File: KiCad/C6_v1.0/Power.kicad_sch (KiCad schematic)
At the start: 35 parts, among them J6 6130XX11121_61300511121, J7 Conn_01x05_Pin

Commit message: pingus
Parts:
- removed C20: WCAP-ASLL_4X5.5/865060640001 1uf smd electrolytic, 865060640001 1uf electrolytic:WCAP-ASLL_4X5.5_DXL_, symbol WCAP-ASLL_4X5.5:WCAP-ASLL_4X5.5
- removed C?: WCAP-ASLI_5X5.5/ 47uf electro, 865080342006 47uf electrolytic:WCAP-ASLI_5X5.5_DXL_, symbol WCAP-ASLI_5X5.5:WCAP-ASLI_5X5.5
- removed J7: Conn_01x05_Pin, Connector_PinHeader_2.00mm:PinHeader_1x05_P2.00mm_Vertical, symbol Connector:Conn_01x05_Pin
- removed Payload_Header?: B02B-XASK-1LFSN, footprints:CONN_B02B-XASK-1LFSN_JST, symbol 2025-10-14_01-11-02:B02B-XASK-1LFSN
- removed Payload_LoadSwitch?: TPS22919DCKR, TPS22919DCKR:SOT65P210X110-6N, symbol TPS22919DCKR:TPS22919DCKR
- removed R33: RC0201FR-0710KL/ 10k, Resistor_SMD:R_0201_0603Metric_Pad0.64x0.40mm_HandSolder, symbol 2025-10-26_02-06-39:RC0201FR-0710KL
- removed R38: RC0402JR-071KL 1k, Resistor_SMD:R_0402_1005Metric_Pad0.72x0.64mm_HandSolder, symbol 2025-10-26_18-21-17:RC0402JR-071KL
- R33: renamed from R?; value 10000 -> 51k
- gave numbers to parts that had none: 17
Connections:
- no-connect marks 3 -> 1
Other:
- moved on the sheet: J6, R33, TP1

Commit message: yay
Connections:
- net +2.8V is gone; now on net 2V8: J6.2
- net +3.3V is gone; now on net 3V3: J6.3
- net +5V is gone; now on net 5V: C35.1, C37.1, Current_Monitor1.1 (A1), Current_Monitor1.2 (A0), Current_Monitor1.5 (VS), J6.4
- net +8.4V is gone; now on net 8V4: J6.5
- net 1.8V is gone; now on net 1V8: J6.1
- net ADC_IN renamed ADC
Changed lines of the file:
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@@
+	(wire
+		(pts
+			(xy 222.25 78.74) (xy 233.68 78.74)
+		)
+		(stroke
+			(width 0)
+			(type default)
+		)
+	)
 	(wire
 		(pts
@@
 	(wire
 		(pts
-			(xy 224.79 81.28) (xy 233.68 81.28)
-		)
-		(stroke
-			(width 0)
-			(type default)
-		)
-	)
-	(wire
-		(pts
 			(xy 185.42 137.16) (xy 201.93 137.16)
 		)
@@
 	(wire
 		(pts
-			(xy 224.79 78.74) (xy 233.68 78.74)
-		)
-		(stroke
-			(width 0)
-			(type default)
-		)
-	)
-	(wire
-		(pts
 			(xy 59.69 146.05) (xy 67.31 146.05)
 		)
@@
 		(pts
 			(xy 49.53 153.67) (xy 49.53 157.48)
+		)
+		(stroke
+			(width 0)
+			(type default)
+		)
+	)
+	(wire
+		(pts
+			(xy 222.25 81.28) (xy 233.68 81.28)
 		)
 		(stroke
@@
 		)
 	)
+	(label "8V4"
+		(at 123.19 30.48 270)
+		(effects
+			(font
+				(size 1.27 1.27)
+			)
+			(justify right bottom)
+		)
+	)
+	(label "2V8"
+		(at 115.57 30.48 270)
+		(effects
+			(font
+				(size 1.27 1.27)
+			)
+			(justify right bottom)
+		)
+	)
+	(label "3V3"
+		(at 118.11 30.48 270)
+		(effects
+			(font
+				(size 1.27 1.27)
+			)
+			(justify right bottom)
+		)
+	)
 	(label "VOUT"
 		(at 231.14 88.9 180)
@@
 		)
 	)
+	(label "1V8"
+		(at 113.03 30.48 270)
+		(effects
+			(font
+				(size 1.27 1.27)
+			)
+			(justify right bottom)
+		)
+	)
+	(label "5V"
+		(at 93.98 73.66 0)
+		(effects
+			(font
+				(size 1.27 1.27)
+			)
+			(justify left bottom)
+		)
+	)
 	(label "bruh"
 		(at 195.58 137.16 0)
@@
 		)
 	)
-	(global_label "EGSE_TX"
-		(shape input)
-		(at 224.79 81.28 180)
-		(fields_autoplaced yes)
-		(effects
-			(font
-				(size 1.27 1.27)
-			)
-			(justify right)
-		)
-		(property "Intersheetrefs" "${INTERSHEET_REFS}"
-			(at 213.8826 81.28 0)
-			(effects
-				(font
-					(size 1.27 1.27)
-				)
-				(justify right)
-				(hide yes)
-			)
-		)
-	)
-	(global_label "+8.4V"
-		(shape input)
-		(at 123.19 30.48 270)
-		(fields_autoplaced yes)
-		(effects
-			(font
-				(size 1.27 1.27)
-			)
-			(justify right)
-		)
-		(property "Intersheetrefs" "${INTERSHEET_REFS}"
-			(at 123.19 39.15 90)
-			(effects
-				(font
-					(size 1.27 1.27)
-				)
-				(justify right)
-				(hide yes)
-			)
-		)
-	)
-	(global_label "I2C_SCL"
-		(shape input)
-		(at 104.14 99.06 0)
-		(fields_autoplaced yes)
-		(effects
-			(font
-				(size 1.27 1.27)
-			)
-			(justify left)
-		)
-		(property "Intersheetrefs" "${INTERSHEET_REFS}"
-			(at 114.6847 99.06 0)
-			(effects
-				(font
-					(size 1.27 1.27)
-				)
-				(justify left)
-				(hide yes)
-			)
-		)
-	)
-	(global_label "EGSE_RX"
-		(shape input)
-		(at 224.79 78.74 180)
-		(fields_autoplaced yes)
-		(effects
-			(font
-				(size 1.27 1.27)
-			)
-			(justify right)
-		)
-		(property "Intersheetrefs" "${INTERSHEET_REFS}"
-			(at 213.5802 78.74 0)
-			(effects
-				(font
-					(size 1.27 1.27)
-				)
-				(justify right)
-				(hide yes)
-			)
-		)
-	)
-	(global_label "+3.3V"
-		(shape input)
-		(at 118.11 30.48 270)
-		(fields_autoplaced yes)
-		(effects
-			(font
-				(size 1.27 1.27)
-			)
-			(justify right)
-		)
-		(property "Intersheetrefs" "${INTERSHEET_REFS}"
-			(at 118.11 39.15 90)
-			(effects
-				(font
-					(size 1.27 1.27)
-				)
-				(justify right)
-				(hide yes)
-			)
-		)
-	)
-	(global_label "+2.8V"
-		(shape input)
-		(at 115.57 30.48 270)
-		(fields_autoplaced yes)
-		(effects
-			(font
-				(size 1.27 1.27)
-			)
-			(justify right)
-		)
-		(property "Intersheetrefs" "${INTERSHEET_REFS}"
-			(at 115.57 39.15 90)
-			(effects
-				(font
-					(size 1.27 1.27)
-				)
-				(justify right)
-				(hide yes)
-			)
-		)
-	)
-	(global_label "+5V"
-		(shape input)
+	(label "5V"
 		(at 120.65 30.48 270)
-		(fields_autoplaced yes)
-		(effects
-			(font
-				(size 1.27 1.27)
-			)
-			(justify right)
-		)
-		(property "Intersheetrefs" "${INTERSHEET_REFS}"
-			(at 120.65 37.3357 90)
-			(effects
-				(font
-					(size 1.27 1.27)
-				)
-				(justify right)
-				(hide yes)
-			)
-		)
-	)
-	(global_label "+5V"
-		(shape input)
-		(at 93.98 73.66 90)
-		(fields_autoplaced yes)
-		(effects
-			(font
-				(size 1.27 1.27)
-			)
-			(justify left)
-		)
-		(property "Intersheetrefs" "${INTERSHEET_REFS}"
-			(at 93.98 66.8043 90)
-			(effects
-				(font
-					(size 1.27 1.27)
-				)
-				(justify left)
-				(hide yes)
-			)
-		)
-	)
-	(global_label "ADC_IN"
-		(shape input)
-		(at 30.48 99.06 0)
-		(fields_autoplaced yes)
-		(effects
-			(font
-				(size 1.27 1.27)
-			)
-			(justify left)
-		)
-		(property "Intersheetrefs" "${INTERSHEET_REFS}"
-			(at 39.9967 99.06 0)
-			(effects
-				(font
-					(size 1.27 1.27)
-				)
-				(justify left)
-				(hide yes)
-			)
-		)
-	)
-	(global_label "1.8V"
-		(shape input)
-		(at 113.03 30.48 270)
-		(fields_autoplaced yes)
-		(effects
-			(font
-				(size 1.27 1.27)
-			)
-			(justify right)
-		)
-		(property "Intersheetrefs" "${INTERSHEET_REFS}"
-			(at 113.03 37.5776 90)
-			(effects
-				(font
-					(size 1.27 1.27)
-				)
-				(justify right)
-				(hide yes)
-			)
+		(effects
+			(font
+				(size 1.27 1.27)
+			)
+			(justify right bottom)
 		)
 	)
@@
 		)
 	)
+	(hierarchical_label "ADC"
+		(shape input)
+		(at 30.48 99.06 0)
+		(effects
+			(font
+				(size 1.27 1.27)
+			)
+			(justify left)
+		)
+	)
 	(hierarchical_label "8V4"
 		(shape input)
@@
 		)
 	)
+	(hierarchical_label "EGSE_TX"
+		(shape input)
+		(at 222.25 81.28 180)
+		(effects
+			(font
+				(size 1.27 1.27)
+			)
+			(justify right)
+		)
+	)
+	(hierarchical_label "EGSE_RX"
+		(shape input)
+		(at 222.25 78.74 180)
+		(effects
+			(font
+				(size 1.27 1.27)
+			)
+			(justify right)
+		)
+	)
 	(hierarchical_label "5V"
 		(shape input)
@@
 		(effects
 			(font
+				(size 1.27 1.27)
+			)
+			(justify left)
+		)
+	)
+	(hierarchical_label "I2C_SCL"
+		(shape input)
+		(at 104.14 99.06 0)
+		(effects
+			(font

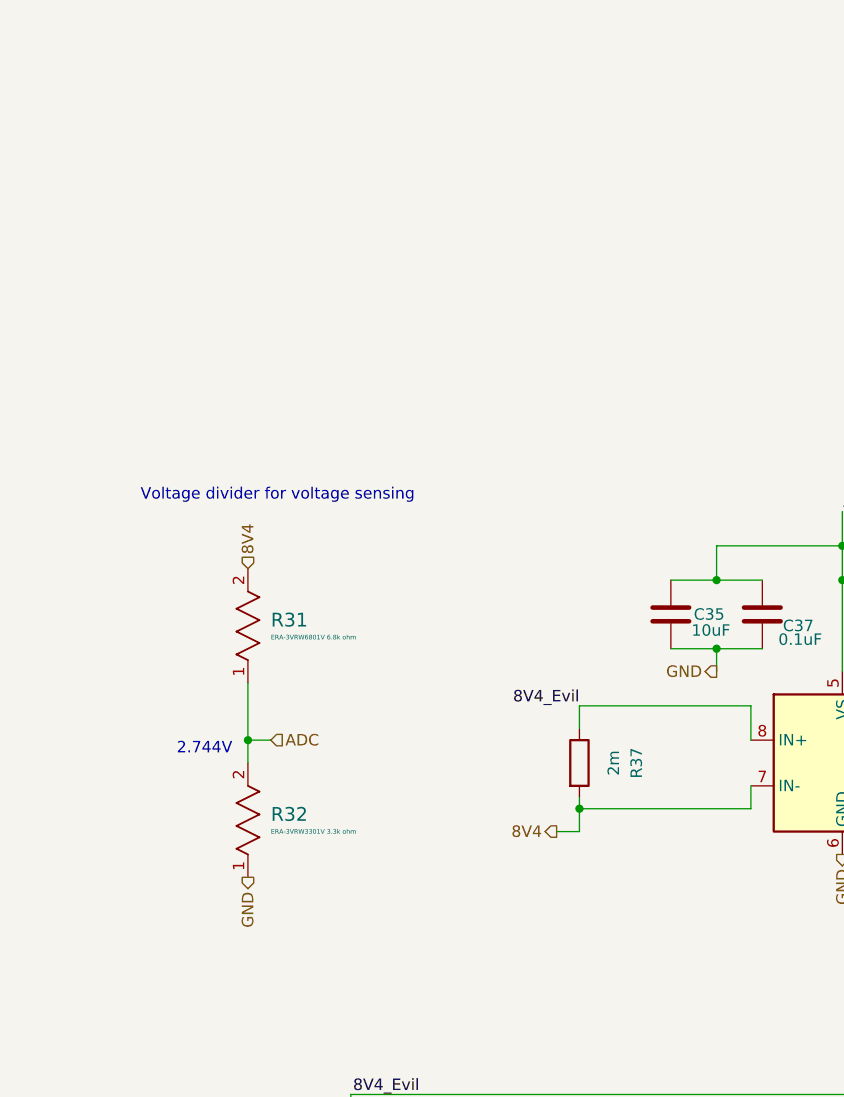
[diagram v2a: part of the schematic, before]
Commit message: made voltage sense more accurate to 1%
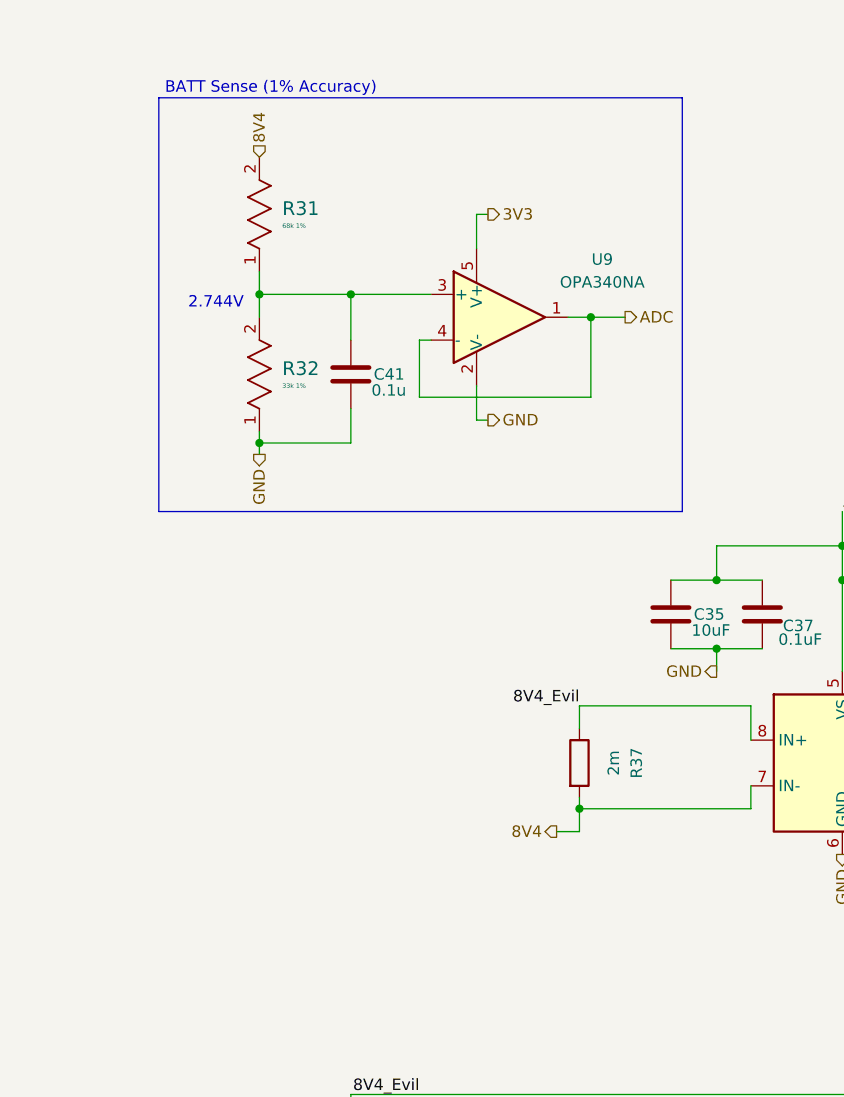
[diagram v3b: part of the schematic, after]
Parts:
- added C41: 0.1u, Capacitor_SMD:C_1206_3216Metric, symbol Device:C
- added U9: OPA340NA, Package_TO_SOT_SMD:SOT-23-5, symbol Amplifier_Operational:OPA340NA
- R31: value ERA-3VRW6801V 6.8k ohm -> 68k 1%
- R32: value ERA-3VRW3301V 3.3k ohm -> 33k 1%
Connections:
- net 3V3: now also U9.5 (V+)
- net ADC: now also U9.1, U9.4 (-); no longer R31.1, R32.2
- net GND: now also C41.2, U9.2 (V-)
- new net: C41.1, R31.1, R32.2, U9.3 (+)
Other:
- note added: "BATT Sense (1% Accuracy)"
- note removed: "Voltage divider for voltage sensing"
- moved on the sheet: R31, R32

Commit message: foot!
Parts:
- removed J6: 6130XX11121_61300511121, Connector_PinHeader_2.54mm:PinHeader_1x05_P2.54mm_Vertical, symbol 6130XX11121_61300511121:6130XX11121_61300511121
- removed TP1: RCWCTE, Connector_PinHeader_2.00mm:PinHeader_1x01_P2.00mm_Vertical, symbol RCWCTE:RCWCTE

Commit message: save
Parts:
- BMS1: footprint BQ29209DRBR Protection IC:DRB8_1P6X2P4 -> BQ29209:DRB8_1P6X2P4
- BatteryConnector1: footprint Footprints:CONN_B03B-XASK-1_JST -> B03B-XASK-1_JST:CONN_B03B-XASK-1_JST
- DSUB1: footprint ICD15S13E4GX00LF dsub:AMPHENOL_ICD15S13E4GX00LF -> ICD15S13E4GX00LF:AMPHENOL_ICD15S13E4GX00LF
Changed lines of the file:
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@@
 			)
 		)
-		(property "Footprint" "Footprints:CONN_B03B-XASK-1_JST"
+		(property "Footprint" "B03B-XASK-1_JST:CONN_B03B-XASK-1_JST"
 			(at 29.21 160.02 0)
 			(effects
@@
 			)
 		)
-		(property "Footprint" "BQ29209DRBR Protection IC:DRB8_1P6X2P4"
+		(property "Footprint" "BQ29209:DRB8_1P6X2P4"
 			(at 78.74 151.13 0)
 			(effects
@@
 			)
 		)
-		(property "Footprint" "ICD15S13E4GX00LF dsub:AMPHENOL_ICD15S13E4GX00LF"
+		(property "Footprint" "ICD15S13E4GX00LF:AMPHENOL_ICD15S13E4GX00LF"
 			(at 246.38 86.36 0)
 			(effects

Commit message: im scared
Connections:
- net GNDD is gone; now on net GND: C39.2
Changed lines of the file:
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@@
 			)
 		)
-		(property "Value" "GNDD"
-			(at 171.45 135.89 0)
+		(property "Value" "GND"
+			(at 173.99 133.1594 0)
 			(effects
 				(font
 					(size 1.27 1.27)
 				)
+				(justify left)
 			)
 		)

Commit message: john d tickle
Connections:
- net GND: now also DSUB1.S1 (SHIELD), DSUB1.S2 (SHIELD__1)
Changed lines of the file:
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@@
+		)
+	)
+	(hierarchical_label "GND"
+		(shape output)
+		(at 233.68 104.14 180)
+		(effects
+			(font
+				(size 1.27 1.27)
+			)
+			(justify right)
 		)
 	)
@@
 		)
 	)
+	(hierarchical_label "GND"
+		(shape output)
+		(at 233.68 101.6 180)
+		(effects
+			(font
+				(size 1.27 1.27)
+			)
+			(justify right)
+		)
+	)

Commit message: sneaky commit
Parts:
- removed BatteryConnector1: B03B-XASK-1, B03B-XASK-1_JST:CONN_B03B-XASK-1_JST, symbol 2025-10-05_21-07-24:B03B-XASK-1
- added J14: Conn_01x03, Connector_JST:JST_XA_S03B-XASK-1_1x03_P2.50mm_Horizontal, symbol Connector_Generic:Conn_01x03
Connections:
- net 8V4_Evil: now also J14.3 (Pin_3)
- net GND: now also J14.1 (Pin_1)
- net at R35.1, R36.1: now also J14.2 (Pin_2)
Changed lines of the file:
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@@
+	)
+	(symbol
+		(lib_id "Connector_Generic:Conn_01x03")
+		(at 24.13 157.48 180)
+		(unit 1)
+		(exclude_from_sim no)
+		(in_bom yes)
+		(on_board yes)
+		(dnp no)
+		(fields_autoplaced yes)
+		(property "Reference" "J14"
+			(at 24.13 148.59 0)
+			(effects
+				(font
+					(size 1.27 1.27)
+				)
+			)
+		)
+		(property "Value" "Conn_01x03"
+			(at 24.13 151.13 0)
+			(effects
+				(font
+					(size 1.27 1.27)
+				)
+			)
+		)
+		(property "Footprint" "Connector_JST:JST_XA_S03B-XASK-1_1x03_P2.50mm_Horizontal"
+			(at 24.13 157.48 0)
+			(effects
+				(font
+					(size 1.27 1.27)
+				)
+				(hide yes)
+			)
+		)
+		(property "Datasheet" "~"
+			(at 24.13 157.48 0)
+			(effects
+				(font
+					(size 1.27 1.27)
+				)
+				(hide yes)
+			)
+		)
+		(property "Description" "Generic connector, single row, 01x03, script generated (kicad-library-utils/schlib/autogen/connector/)"
+			(at 24.13 157.48 0)
+			(effects
+				(font
+					(size 1.27 1.27)
+				)
+				(hide yes)
+			)
+		)
+		(pin "3"
+		)
+		(pin "1"
+		)
+		(pin "2"
+		)
+		(instances
+			(project "C6v1.0"
+				(path "/8737aa07-2805-4383-a805-a4fb57529a3e/4d3c3eea-62ea-4a75-81f8-713bd295f2ea"
+					(reference "J14")
+					(unit 1)
+				)
+			)
+		)
 	)
 	(symbol
@@
 					(unit 1)
 				)
-			)
-		)
-	)
-	(symbol
-		(lib_id "2025-10-05_21-07-24:B03B-XASK-1")
-		(at 29.21 160.02 180)
-		(unit 1)
-		(exclude_from_sim no)
-		(in_bom yes)
-		(on_board yes)
-		(dnp no)
-		(property "Reference" "BatteryConnector1"
-			(at 27.686 147.828 0)
-			(effects
-				(font
-					(size 1.524 1.524)
-				)
-				(justify left)
-			)
-		)
-		(property "Value" "B03B-XASK-1"
-			(at 26.162 150.114 0)
-			(effects
-				(font
-					(size 1.524 1.524)
-				)
-				(justify left)
-			)
-		)
-		(property "Footprint" "B03B-XASK-1_JST:CONN_B03B-XASK-1_JST"
-			(at 29.21 160.02 0)
-			(effects
-				(font
-					(size 1.27 1.27)
-					(italic yes)
-				)
-				(hide yes)
-			)
-		)
-		(property "Datasheet" "B03B-XASK-1"
-			(at 29.21 160.02 0)
-			(effects
-				(font
-					(size 1.27 1.27)
-					(italic yes)
-				)
-				(hide yes)
-			)
-		)
-		(property "Description" ""
-			(at 29.21 160.02 0)
-			(effects
-				(font
-					(size 1.27 1.27)
-				)
-				(hide yes)
-			)
-		)
-		(pin "2"
-		)
-		(pin "3"
-		)
-		(pin "1"
-		)
-		(instances
-			(project "C6v1.0"
-				(path "/8737aa07-2805-4383-a805-a4fb57529a3e/4d3c3eea-62ea-4a75-81f8-713bd295f2ea"
-					(reference "BatteryConnector1")
-					(unit 1)
-				)
